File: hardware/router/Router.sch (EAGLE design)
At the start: 35 parts, among them IC1 ATMEGA165A, J1 AVR_SPI_PRG_62X3_LOCK, J10 RJ45-8PTH, J11 RJ45-8PTH, J12 RJ45-8PTH, J13 RJ45-8PTH, J14 RJ45-8PTH, J15 RJ45-8PTH, J16 RJ45-8PTH, J2 RJ45-8PTH, J3 RJ45-8PTH, J4 RJ45-8PTH, J5 RJ45-8PTH, J6 RJ45-8PTH, J7 RJ45-8PTH, J8 RJ45-8PTH, J9 RJ45-8PTH, U1 WS2801, U2 VREG-5V-LDO-AP1117SOT89-3L

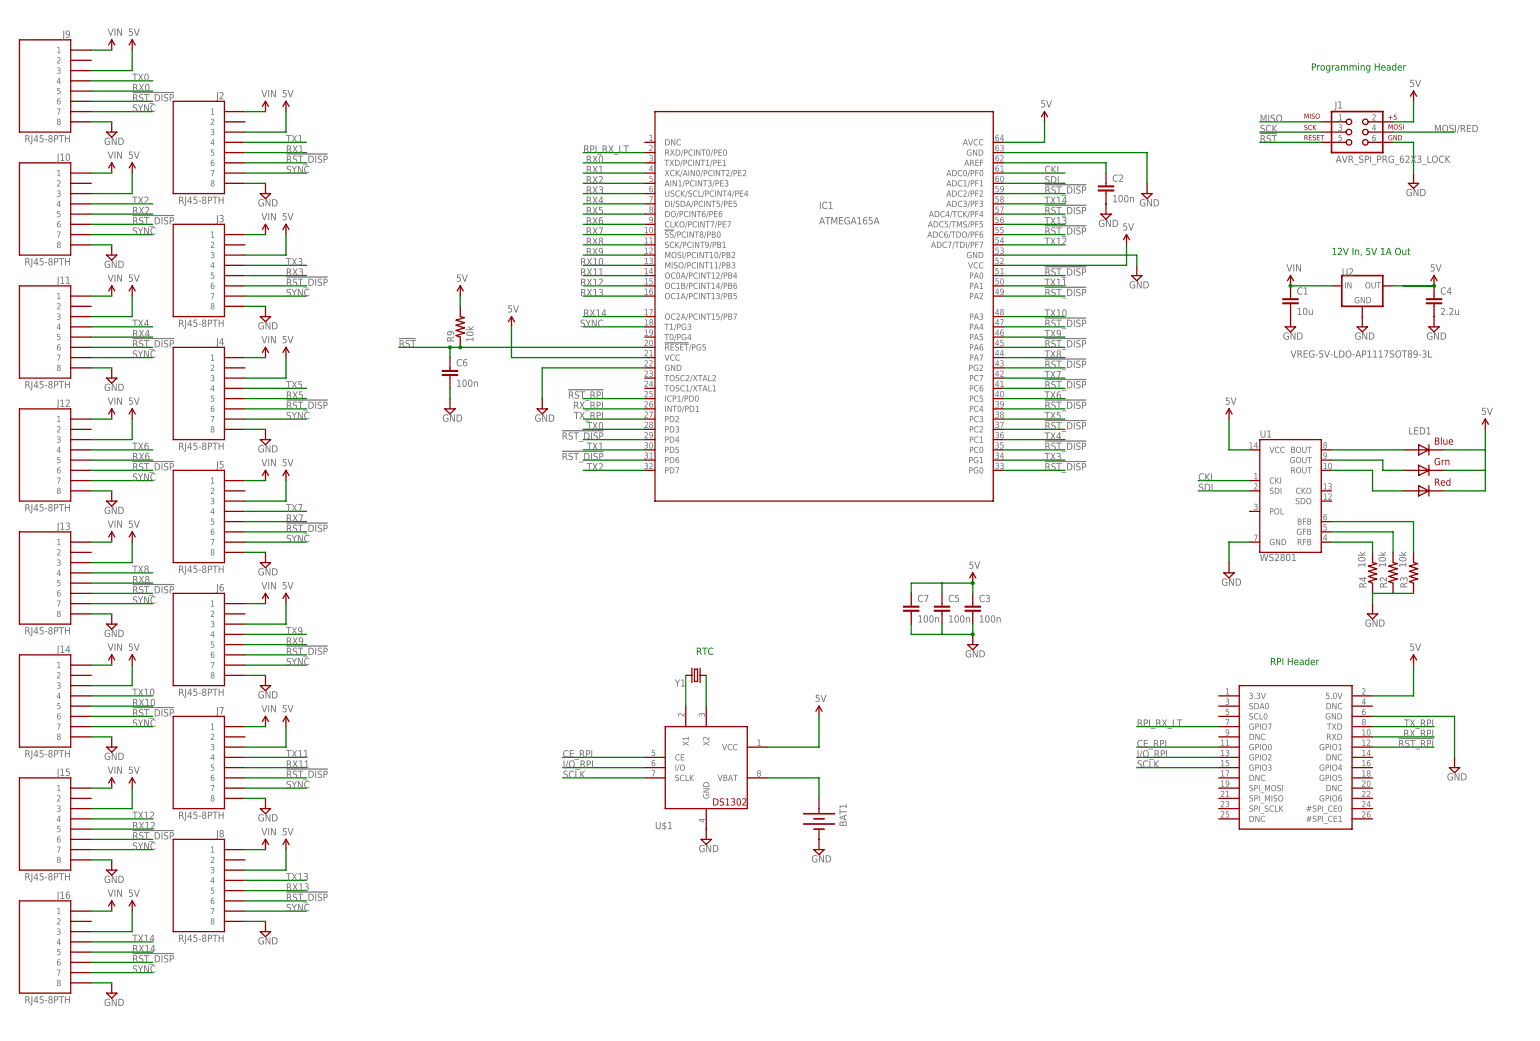
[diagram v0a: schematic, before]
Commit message: Updated Router with the latest pinouts from Rob after breadboard testing 12/28/12
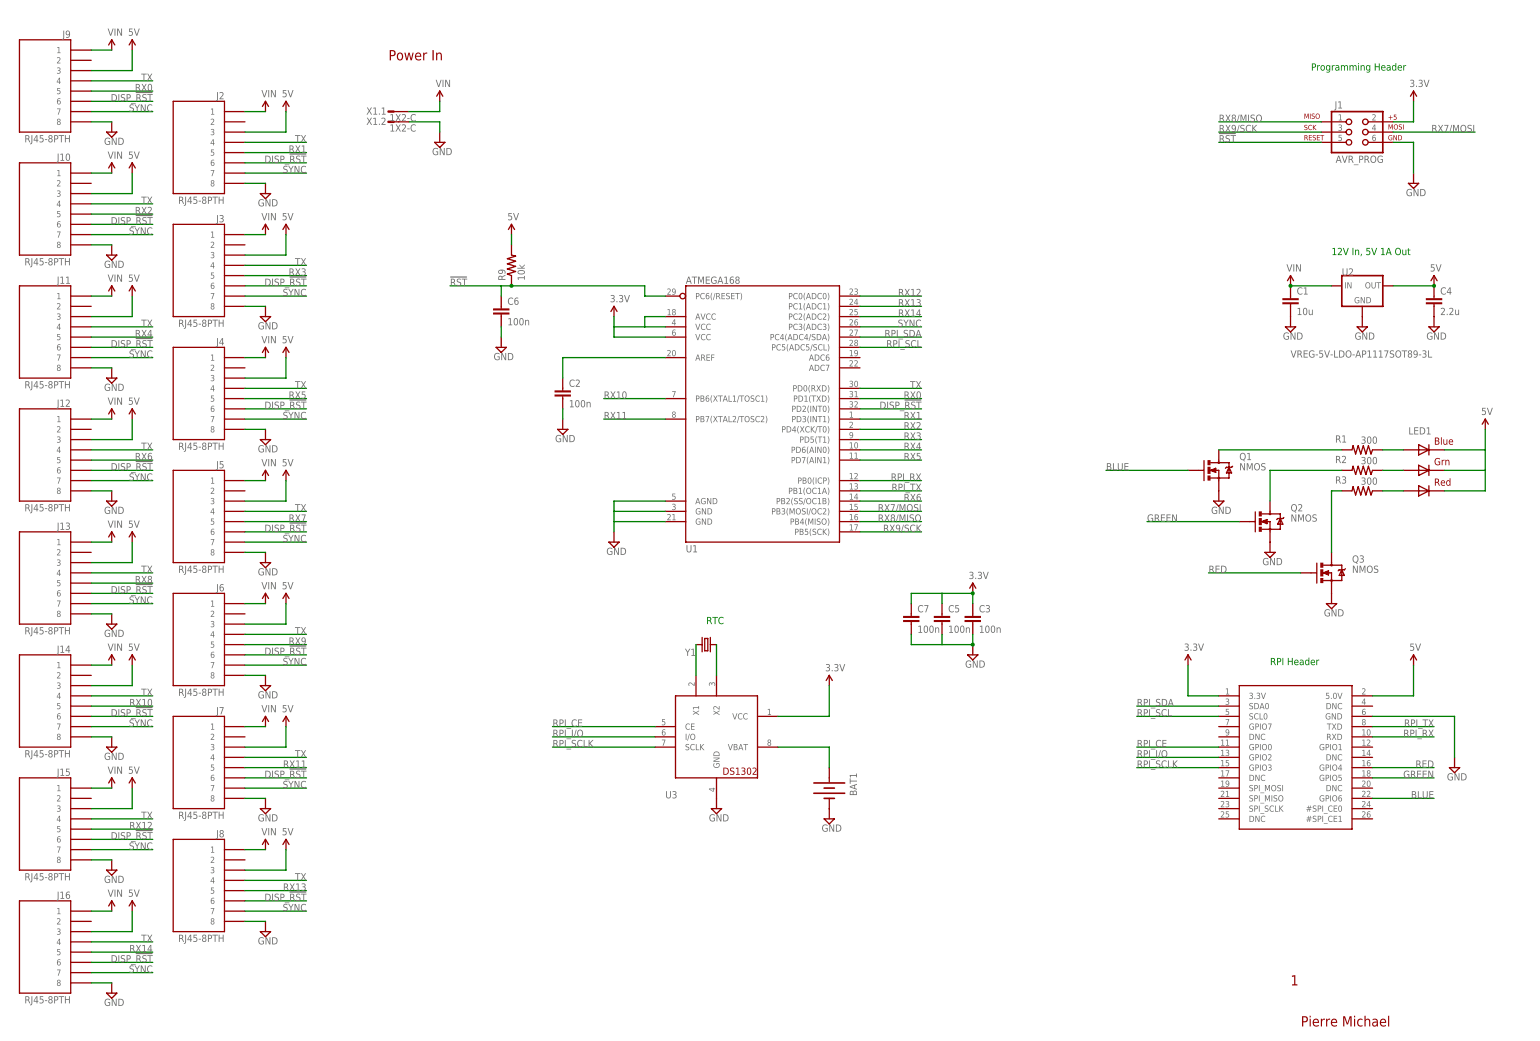
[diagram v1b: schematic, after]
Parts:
- removed IC1: ATMEGA165A, pierre:ATMEGA165A
- removed R4: 10k, SparkFun-Resistors:RESISTOR0603-RES
- removed U$1: DS1302_SMT, pierre:DS1302_SMT
- added Q1, Q2, Q3: NMOS, SparkFun-DiscreteSemi:MOSFET-NCHANNELSMD
- added R1: 300, SparkFun-Resistors:RESISTOR0603-RES
- added U3: DS1302_SMT, pierre:DS1302_SMT
- added X1: 1X2-C, con-amp-micro-mate-n-lock:1X2-C
- J1: value AVR_SPI_PRG_62X3_LOCK -> AVR_PROG
- R2, R3: value 10k -> 300
- U1: value WS2801 -> ATMEGA168; device SparkFun-DigitalIC:WS2801 -> SparkFun-DigitalIC:ATMEGA168
- renumbered U$38 to J17
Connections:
- removed net !RST_DISP: J10.6, J11.6, J12.6, J13.6, J14.6, J15.6, J16.6, J2.6, J3.6, J4.6, J5.6, J6.6, J7.6, J8.6, J9.6
- removed net CE_RPI: J17.GPIO0, U$1.CE
- removed net CKI: IC1.ADC0/PF0, U1.CKI
- removed net I/O_RPI: J17.GPIO2, U$1.I/O
- removed net MISO: J1.1
- removed net MOSI/RED: J1.4
- removed net N$5: J17.GPIO1
- removed net RPI_RX_LT: IC1.RXD/PCINT0/PE0, J17.GPIO7
- removed net SCK: J1.3
- removed net SCLK: J17.GPIO3, U$1.SCLK
- removed net SDI: IC1.ADC1/PF1, U1.SDI
- removed net TX0: J9.4
- removed net TX1: J2.4
- removed net TX10: J14.4
- removed net TX11: J7.4
- removed net TX12: J15.4
- removed net TX13: J8.4
- removed net TX14: J16.4
- removed net TX2: J10.4
- removed net TX3: J3.4
- removed net TX4: J11.4
- removed net TX5: J4.4
- removed net TX6: J12.4
- removed net TX7: J5.4
- removed net TX8: J13.4
- removed net TX9: J6.4
- new net BLUE: J17.GPIO6, Q1.G
- new net DISP_!RST: J10.6, J11.6, J12.6, J13.6, J14.6, J15.6, J16.6, J2.6, J3.6, J4.6, J5.6, J6.6, J7.6, J8.6, J9.6, U1.PD2(INT0)
- new net GREEN: J17.GPIO5, Q2.G
- new net N$16: U1.AGND
- new net N$17: U1.GND@2
- new net N$8: U1.AVCC, U1.VCC@1
- new net RED: J17.GPIO4, Q3.G
- new net RPI_CE: J17.GPIO0, U3.CE
- new net RPI_I/O: J17.GPIO2, U3.I/O
- new net RPI_RX: U1.PB0(ICP)
- new net RPI_SCL: J17.SCL0, U1.PC5(ADC5/SCL)
- new net RPI_SCLK: J17.GPIO3, U3.SCLK
- new net RPI_SDA: J17.SDA0, U1.PC4(ADC4/SDA)
- new net RPI_TX: U1.PB1(OC1A)
- new net RX7/MOSI: J1.4, U1.PB3(MOSI/OC2)
- new net RX8/MISO: J1.1, U1.PB4(MISO)
- new net RX9/SCK: J1.3, U1.PB5(SCK)
- new net TX: J10.4, J11.4, J12.4, J13.4, J14.4, J15.4, J16.4, J2.4, J3.4, J4.4, J5.4, J6.4, J7.4, J8.4, J9.4, U1.PD0(RXD)
- new net VIN: X1.1.S
- net !RST: now also U1.PC6(/RESET)
- net 5V: now also J17.3.3V@1, U1.VCC@2, U3.VCC; no longer IC1.VCC, IC1.VCC@1, U$1.VCC, U1.VCC
- net GND: now also Q1.S, Q2.S, Q3.S, U1.GND@1, U3.GND, X1.2.S; no longer IC1.GND, IC1.GND@2, R2.1, R3.1, R4.1, U$1.GND, U1.GND
- net N$1: now also U3.VBAT; no longer U$1.VBAT
- net N$10: now also Q1.D, R1.2; no longer LED1.GREEN_A, U1.GOUT
- net N$11: now also Q2.D, R2.2; no longer LED1.RED_A, U1.ROUT
- net N$12: now also LED1.GREEN_A, R2.1; no longer R4.2, U1.RFB
- net N$13: now also LED1.RED_A, R3.1; no longer R2.2, U1.GFB
- net N$14: now also Q3.D; no longer U1.BFB
- net N$4: now also U1.AREF; no longer IC1.AREF
- net N$6: now also U3.X2; no longer U$1.X2
- net N$7: now also U3.X1; no longer U$1.X1
- net N$9: now also R1.1; no longer U1.BOUT
- net RX0: now also U1.PD1(TXD)
- net RX1: now also U1.PD3(INT1)
- net RX10: now also U1.PB6(XTAL1/TOSC1)
- net RX11: now also U1.PB7(XTAL2/TOSC2)
- net RX12: now also U1.PC0(ADC0)
- net RX13: now also U1.PC1(ADC1)
- net RX14: now also U1.PC2(ADC2); no longer IC1.OC2A/PCINT15/PB7
- net RX2: now also U1.PD4(XCK/T0)
- net RX3: now also U1.PD5(T1)
- net RX4: now also U1.PD6(AIN0)
- net RX5: now also U1.PD7(AIN1)
- net RX6: now also U1.PB2(SS/OC1B)
- net SYNC: now also U1.PC3(ADC3)
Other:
- note added: "1"
- note added: "Pierre Michael"
- note added: "Power In"
- moved on the sheet: BAT1, C2, C3, C5, C6, C7, R2, R3, R9, Y1

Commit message: Added Dispenser Schematic and Layout
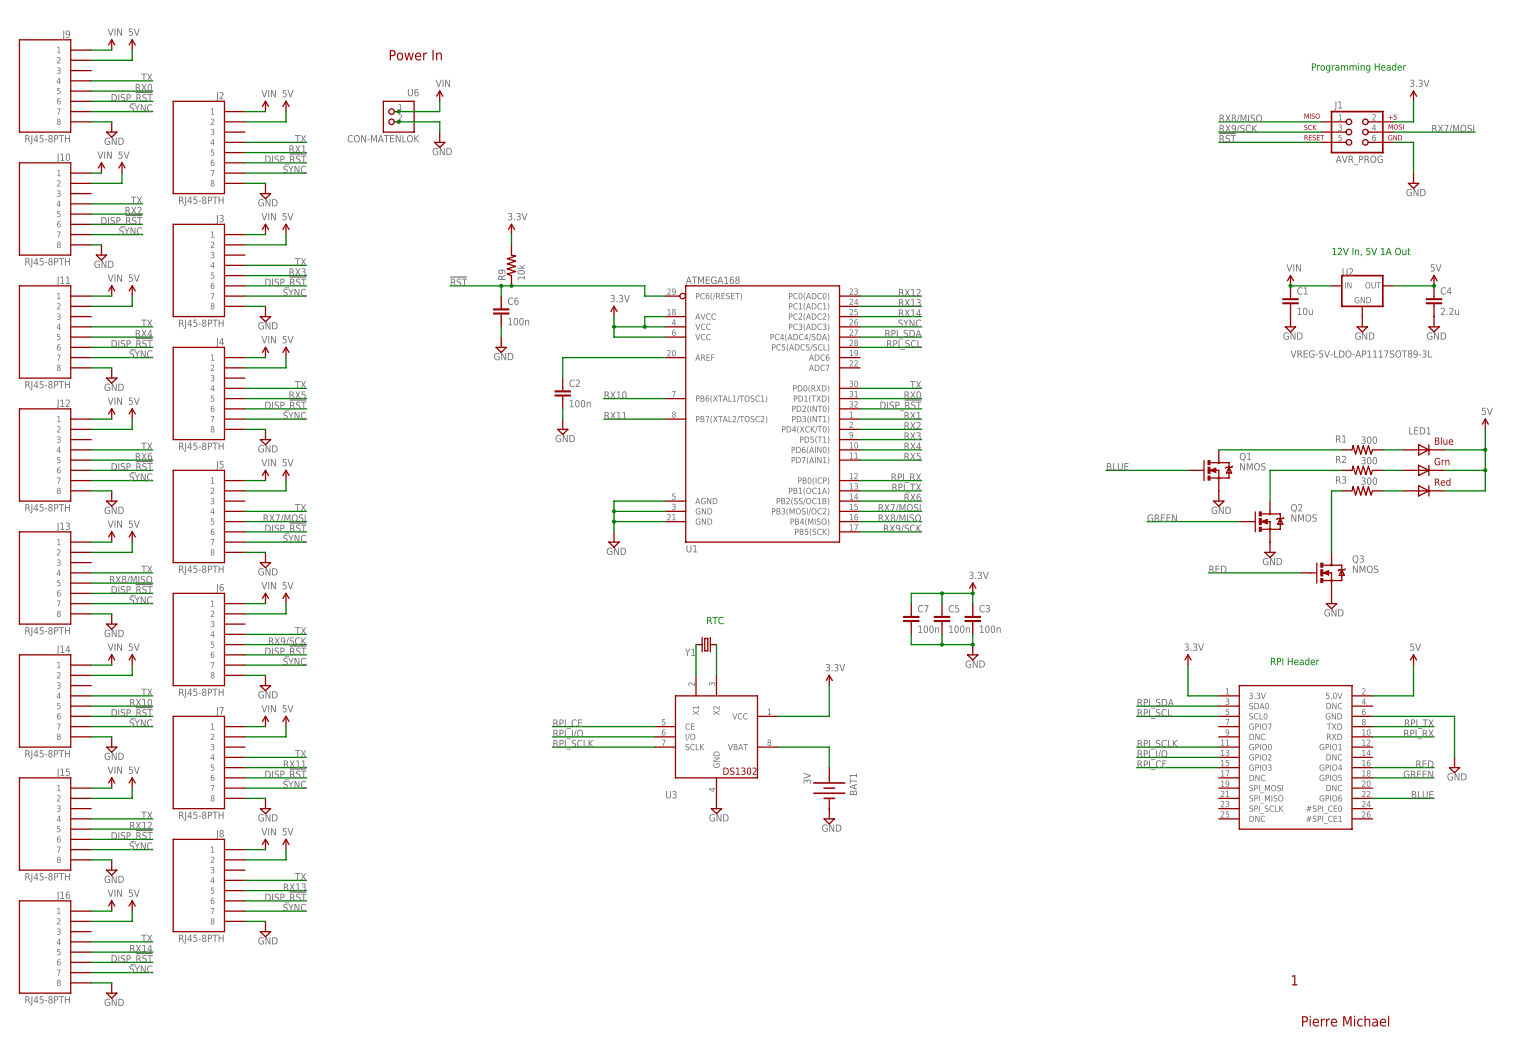
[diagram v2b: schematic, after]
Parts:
- removed X1: 1X2-C, con-amp-micro-mate-n-lock:1X2-C
- added U6: CON-MATENLOK, pierre:CON-MATENLOK
- BAT1: value (none) -> 3V; device SparkFun-Electromechanical:BATTERY20SMD -> SparkFun-Electromechanical:BATTERY12PTH
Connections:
- net N$1 renamed BAT1+
- removed net MOT_A: C1.1, J10.1, J11.1, J12.1, J13.1, J14.1, J15.1, J16.1, J2.1, J3.1, J4.1, J5.1, J6.1, J7.1, J8.1, J9.1, U2.IN
- removed net N$16: U1.AGND
- removed net N$17: U1.GND@2
- removed net N$2: J17.TXD
- removed net N$3: J17.RXD
- removed net N$8: U1.AVCC, U1.VCC@1
- removed net RX7: J5.5
- removed net RX8: J13.5
- removed net RX9: J6.5
- new net 3.3V: C3.1, C5.1, C7.1, J1.2, J17.3.3V@1, R9.2, U1.AVCC, U1.VCC@1, U1.VCC@2, U3.VCC
- net 5V: now also J10.2, J11.2, J12.2, J13.2, J14.2, J15.2, J16.2, J2.2, J3.2, J4.2, J5.2, J6.2, J7.2, J8.2, J9.2; no longer C3.1, C5.1, C7.1, J1.2, J10.3, J11.3, J12.3, J13.3, J14.3, J15.3, J16.3, J17.3.3V@1, J2.3, J3.3, J4.3, J5.3, J6.3, J7.3, J8.3, J9.3, R9.2, U1.VCC@2, U3.VCC
- net GND: now also U1.AGND, U1.GND@2, U6.2; no longer X1.2.S
- net RPI_CE: now also J17.GPIO3; no longer J17.GPIO0
- net RPI_RX: now also J17.RXD
- net RPI_SCLK: now also J17.GPIO0; no longer J17.GPIO3
- net RPI_TX: now also J17.TXD
- net RX7/MOSI: now also J5.5
- net RX8/MISO: now also J13.5
- net RX9/SCK: now also J6.5
- net SYNC: now also J10.7, J11.7, J12.7, J13.7, J14.7, J15.7, J16.7, J2.7, J3.7, J4.7, J5.7, J6.7, J7.7, J8.7
- net VIN: now also C1.1, J10.1, J11.1, J12.1, J13.1, J14.1, J15.1, J16.1, J2.1, J3.1, J4.1, J5.1, J6.1, J7.1, J8.1, J9.1, U2.IN, U6.1; no longer X1.1.S

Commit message: Updated Router Schematic with DS1307 and Accessory Port
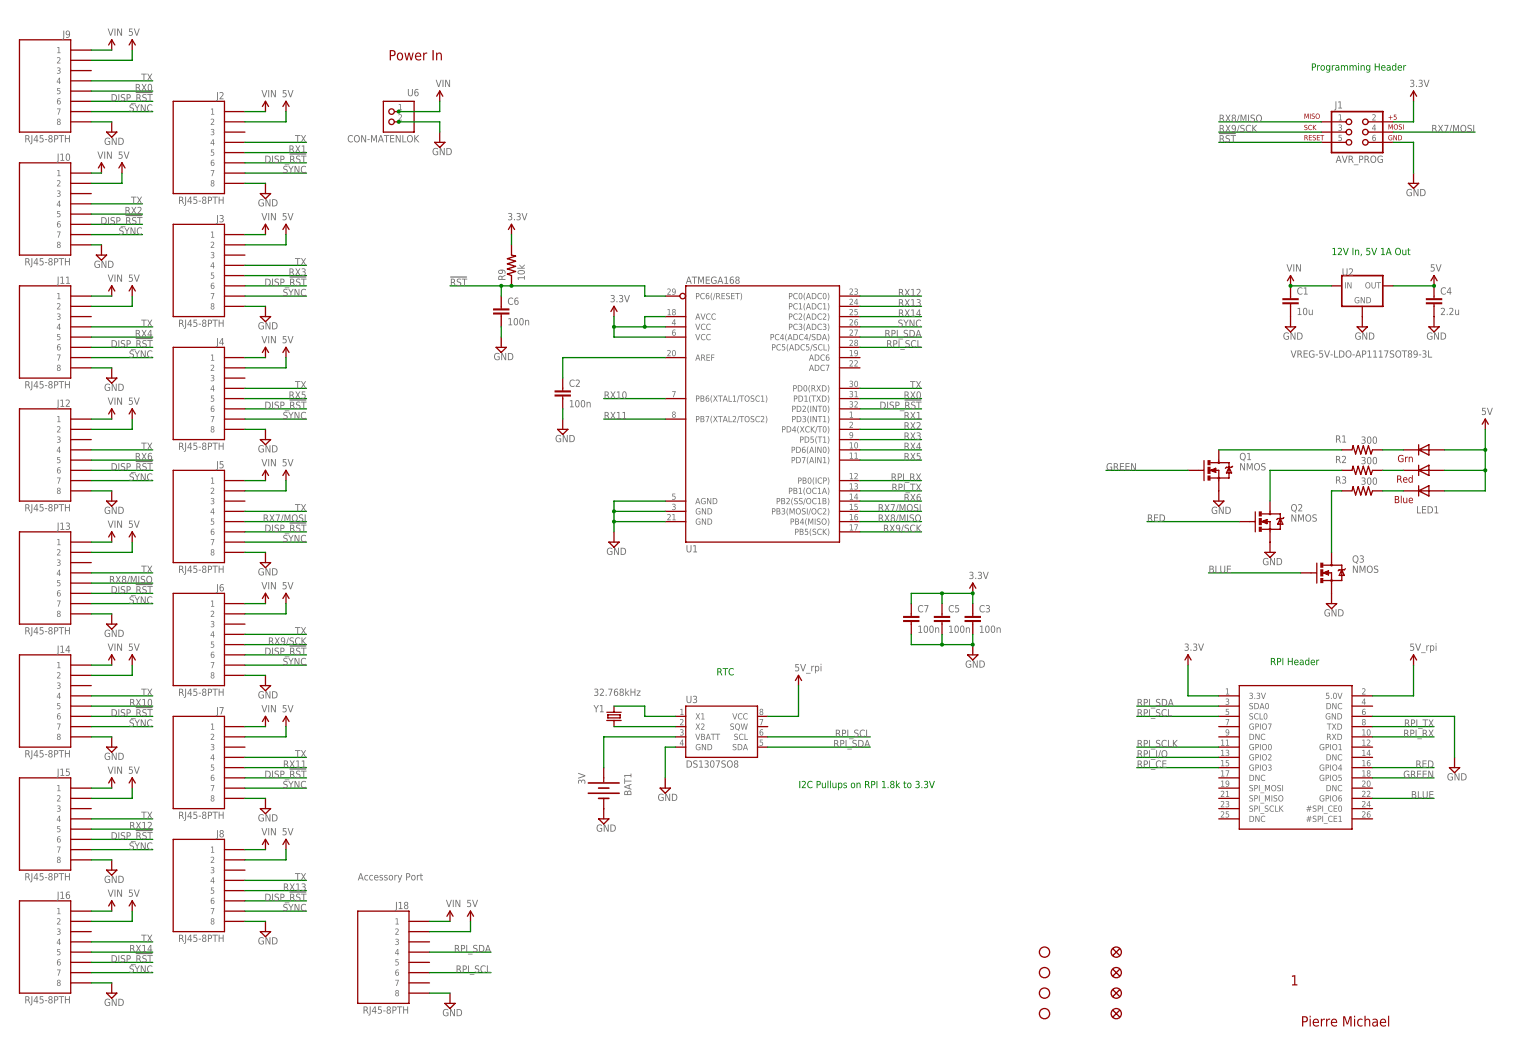
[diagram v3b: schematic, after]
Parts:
- added J18: RJ45-8PTH, SparkFun:RJ45-8PTH
- added JP1, JP2, JP3, JP4: FIDUCIAL1.5X3, SparkFun-Aesthetics:FIDUCIAL1.5X3
- added JP5, JP6, JP7, JP8: STAND-OFFTIGHT, SparkFun-Electromechanical:STAND-OFFTIGHT
- LED1: device adafruit:RGBLED5050 -> pierre:RGBLED5050
- U3: value DS1302_SMT -> DS1307SO8; device pierre:DS1302_SMT -> SparkFun-FreqCtrl:DS1307SO8
- Y1: value (none) -> 32.768kHz
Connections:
- net 3.3V: no longer U3.VCC
- net 5V: now also J18.2, LED1.BLUE_A, LED1.GREEN_A, LED1.RED_A; no longer LED1.BLUE_C, LED1.GREEN_C, LED1.RED_C
- net BAT1+: no longer U3.VBAT
- net BLUE: now also Q3.G; no longer Q1.G
- net GND: now also J18.8
- net GREEN: now also Q1.G; no longer Q2.G
- net N$12: now also LED1.RED_C; no longer LED1.GREEN_A
- net N$13: now also LED1.BLUE_C; no longer LED1.RED_A
- net N$6: now also U3.X1; no longer U3.X2
- net N$7: no longer U3.X1
- net N$9: now also LED1.GREEN_C; no longer LED1.BLUE_A
- net RED: now also Q2.G; no longer Q3.G
- net RPI_CE: no longer U3.CE
- net RPI_I/O: no longer U3.I/O
- net RPI_SCL: now also J18.6, U3.SCL
- net RPI_SCLK: no longer U3.SCLK
- net RPI_SDA: now also J18.4, U3.SDA
- net VIN: now also J18.1
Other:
- note added: "Accessory Port"
- note added: "I2C Pullups on RPI 1.8k to 3.3V"
- moved on the sheet: BAT1, LED1, Y1

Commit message: Commiting updated SCH and BRD
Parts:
- removed JP6: STAND-OFFTIGHT, SparkFun-Electromechanical:STAND-OFFTIGHT
- added C8: 47u, SparkFun-Capacitors:CAP_POLD
- added C9: 100n, SparkFun:CAP0603-CAP
- added FRAME3: FRAME-LETTER, SparkFun-Aesthetics:FRAME-LETTER
- added J19: RJ45-8PTH, SparkFun:RJ45-8PTH
- added JP9: STAND-OFFTIGHT, SparkFun-Electromechanical:STAND-OFFTIGHT
- added U$5: OSHW-LOGOS, SparkFun-Aesthetics:OSHW-LOGOS
- U2: value VREG-5V-LDO-AP1117SOT89-3L -> (none); device pierre:VREG-5V-LDO-AP1117SOT89-3L -> SparkFun-PowerIC:V_REG_78XXSIDE
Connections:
- removed net N$7: Y1.2
- removed net RPI_CE: J17.GPIO3
- removed net RPI_I/O: J17.GPIO2
- new net CE0: J17.#SPI_CE0, J18.7
- new net CE1: J17.#SPI_CE1, J19.7
- new net N$1: U3.X2, Y1.1
- new net RPI_MISO: J17.SPI_MISO, J18.4, J19.4
- new net RPI_MOSI: J17.SPI_MOSI, J18.5, J19.5
- net 5V: now also J19.2, U3.VCC
- net BAT1+: now also U3.VBATT
- net BLUE: now also J17.GPIO4; no longer J17.GPIO6
- net GND: now also C8.-, C9.2, J19.8
- net GREEN: now also J17.GPIO6; no longer J17.GPIO5
- net N$6: now also Y1.2; no longer Y1.1
- net RED: now also J17.GPIO5; no longer J17.GPIO4
- net RPI_SCL: no longer J18.6
- net RPI_SCLK: now also J17.SPI_SCLK, J18.6, J19.6; no longer J17.GPIO0
- net RPI_SDA: no longer J18.4
- net VIN: now also C8.+, C9.1, J19.1
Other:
- note added: "5V 2A Out"
- note added: "Accessory Port 0"
- note added: "Accessory Port 1"
- note added: "Party Robotics (pmichael)"
- note removed: "12V In, 5V 1A Out"
- note removed: "Accessory Port"
- note removed: "Pierre Michael"
- moved on the sheet: BAT1, C1, C4, J1, LED1, Q1, Q2, Q3, R1, R2, R3, U2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

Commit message: Finished Router Layout!
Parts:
- J17: device microbuilder:RASPBERRYPI_BB -> pierre:RASPBERRYPI_BB
